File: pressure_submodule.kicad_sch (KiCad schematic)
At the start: 20 parts, among them IC11 PINA350ABSIDDFR, J13 Conn_01x04, Q11 BSZ0902NSATMA1

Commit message: WIP
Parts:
- renumbered C30 to C23, D12 to D5, F21 to F7, F22 to F8, IC11 to IC4, J13 to J6, JP71 to JP22, JP72 to JP23, JP73 to JP24, JP74 to JP25, JP75 to JP26, JP76 to JP27, JP77 to JP28, Q11 to Q4, R61 to R19, R62 to R20, R63 to R21, R64 to R22, R65 to R23, R66 to R24
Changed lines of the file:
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@@
   (symbol (lib_id "Device:R") (at 55.372 105.41 0)
     (in_bom yes) (on_board yes)
-    (property "Reference" "R63" (id 0) (at 51.562 105.283 0)
+    (property "Reference" "R21" (id 0) (at 51.562 105.283 0)
       (effects (font (size 1.27 1.27)) (justify left))
     )
@@
   (symbol (lib_id "TXV_Library_Symbols:BSZ0902NSATMA1") (at 162.052 74.549 0)
     (in_bom yes) (on_board yes)
-    (property "Reference" "Q11" (id 0) (at 165.989 74.549 0)
+    (property "Reference" "Q4" (id 0) (at 165.989 74.549 0)
       (effects (font (size 1.27 1.27)) (justify left))
     )
@@
   (symbol (lib_id "Jumper:Jumper_2_Open") (at 191.008 63.373 90)
     (in_bom yes) (on_board yes)
-    (property "Reference" "JP75" (id 0) (at 187.833 64.643 0)
+    (property "Reference" "JP26" (id 0) (at 187.833 64.643 0)
       (effects (font (size 1.27 1.27)) (justify left))
     )
@@
   (symbol (lib_id "Device:Polyfuse") (at 186.182 49.403 0)
     (in_bom yes) (on_board yes) (fields_autoplaced)
-    (property "Reference" "F21" (id 0) (at 188.595 48.1329 0)
+    (property "Reference" "F7" (id 0) (at 188.595 48.1329 0)
       (effects (font (size 1.27 1.27)) (justify left))
     )
@@
   (symbol (lib_id "TXV_Library_Symbols:PINA350ABSIDDFR") (at 99.822 92.075 180)
     (in_bom yes) (on_board yes) (fields_autoplaced)
-    (property "Reference" "IC11" (id 0) (at 85.852 76.962 0))
+    (property "Reference" "IC4" (id 0) (at 85.852 76.962 0))
     (property "Value" "PINA350ABSIDDFR" (id 1) (at 85.852 79.502 0))
     (property "Footprint" "TXV_Library_Footprints:SOT65P280X110-8N" (id 2) (at 75.692 94.615 0)
@@
   (symbol (lib_id "Jumper:Jumper_2_Open") (at 101.854 97.155 90)
     (in_bom yes) (on_board yes)
-    (property "Reference" "JP71" (id 0) (at 98.679 98.425 0)
+    (property "Reference" "JP22" (id 0) (at 98.679 98.425 0)
       (effects (font (size 1.27 1.27)) (justify left))
     )
@@
   (symbol (lib_id "Device:R") (at 163.322 91.567 0)
     (in_bom yes) (on_board yes)
-    (property "Reference" "R66" (id 0) (at 158.242 90.297 0)
+    (property "Reference" "R24" (id 0) (at 158.242 90.297 0)
       (effects (font (size 1.27 1.27)) (justify left))
     )
@@
   (symbol (lib_id "Device:C") (at 43.434 105.283 0)
     (in_bom yes) (on_board yes)
-    (property "Reference" "C30" (id 0) (at 39.37 103.505 0)
+    (property "Reference" "C23" (id 0) (at 39.37 103.505 0)
       (effects (font (size 1.27 1.27)) (justify left))
     )
@@
   (symbol (lib_id "Jumper:Jumper_2_Open") (at 191.008 73.533 90)
     (in_bom yes) (on_board yes)
-    (property "Reference" "JP76" (id 0) (at 187.833 74.803 0)
+    (property "Reference" "JP27" (id 0) (at 187.833 74.803 0)
       (effects (font (size 1.27 1.27)) (justify left))
     )
@@
   (symbol (lib_id "Jumper:Jumper_2_Open") (at 143.256 89.535 0)
     (in_bom yes) (on_board yes)
-    (property "Reference" "JP74" (id 0) (at 141.986 86.36 0)
+    (property "Reference" "JP25" (id 0) (at 141.986 86.36 0)
       (effects (font (size 1.27 1.27)) (justify left))
     )
@@
   (symbol (lib_id "Device:R") (at 143.637 74.549 90)
     (in_bom yes) (on_board yes)
-    (property "Reference" "R64" (id 0) (at 143.002 72.644 90)
+    (property "Reference" "R22" (id 0) (at 143.002 72.644 90)
       (effects (font (size 1.27 1.27)) (justify left))
     )
@@
   (symbol (lib_id "Jumper:Jumper_2_Open") (at 106.172 58.293 0)
     (in_bom yes) (on_board yes)
-    (property "Reference" "JP72" (id 0) (at 104.902 55.118 0)
+    (property "Reference" "JP23" (id 0) (at 104.902 55.118 0)
       (effects (font (size 1.27 1.27)) (justify left))
     )
@@
   (symbol (lib_id "Jumper:Jumper_2_Open") (at 113.03 64.643 90)
     (in_bom yes) (on_board yes)
-    (property "Reference" "JP73" (id 0) (at 109.855 65.913 0)
+    (property "Reference" "JP24" (id 0) (at 109.855 65.913 0)
       (effects (font (size 1.27 1.27)) (justify left))
     )
@@
   (symbol (lib_id "Device:D") (at 170.942 73.914 270)
     (in_bom yes) (on_board yes)
-    (property "Reference" "D12" (id 0) (at 172.9486 72.7456 90)
+    (property "Reference" "D5" (id 0) (at 172.9486 72.7456 90)
       (effects (font (size 1.27 1.27)) (justify left))
     )
@@
   (symbol (lib_id "Device:Polyfuse") (at 200.152 49.403 0)
     (in_bom yes) (on_board yes) (fields_autoplaced)
-    (property "Reference" "F22" (id 0) (at 202.565 48.1329 0)
+    (property "Reference" "F8" (id 0) (at 202.565 48.1329 0)
       (effects (font (size 1.27 1.27)) (justify left))
     )
@@
   (symbol (lib_id "Connector_Generic:Conn_01x04") (at 213.106 58.293 0)
     (in_bom yes) (on_board yes)
-    (property "Reference" "J13" (id 0) (at 215.138 58.4962 0)
+    (property "Reference" "J6" (id 0) (at 215.138 58.4962 0)
       (effects (font (size 1.27 1.27)) (justify left))
     )
@@
   (symbol (lib_id "Device:R") (at 151.892 79.629 0)
     (in_bom yes) (on_board yes)
-    (property "Reference" "R65" (id 0) (at 145.542 78.359 0)
+    (property "Reference" "R23" (id 0) (at 145.542 78.359 0)
       (effects (font (size 1.27 1.27)) (justify left))
     )
@@
   (symbol (lib_id "Device:R") (at 55.372 95.25 0)
     (in_bom yes) (on_board yes)
-    (property "Reference" "R62" (id 0) (at 50.292 93.345 0)
+    (property "Reference" "R20" (id 0) (at 50.292 93.345 0)
       (effects (font (size 1.27 1.27)) (justify left))
     )
@@
   (symbol (lib_id "Jumper:Jumper_2_Open") (at 204.216 69.977 90)
     (in_bom yes) (on_board yes)
-    (property "Reference" "JP77" (id 0) (at 201.041 71.247 0)
+    (property "Reference" "JP28" (id 0) (at 201.041 71.247 0)
       (effects (font (size 1.27 1.27)) (justify left))
     )
@@
   (symbol (lib_id "Device:R") (at 49.53 100.457 90)
     (in_bom yes) (on_board yes)
-    (property "Reference" "R61" (id 0) (at 50.292 102.489 90)
-      (effects (font (size 1.27 1.27)) (justify left))
-    )
+    (property "Reference" "R19" (id 0) (at 50.292 102.489 90)
+      (effects (font (size 1.27 1.27)) (justify left))
+    )

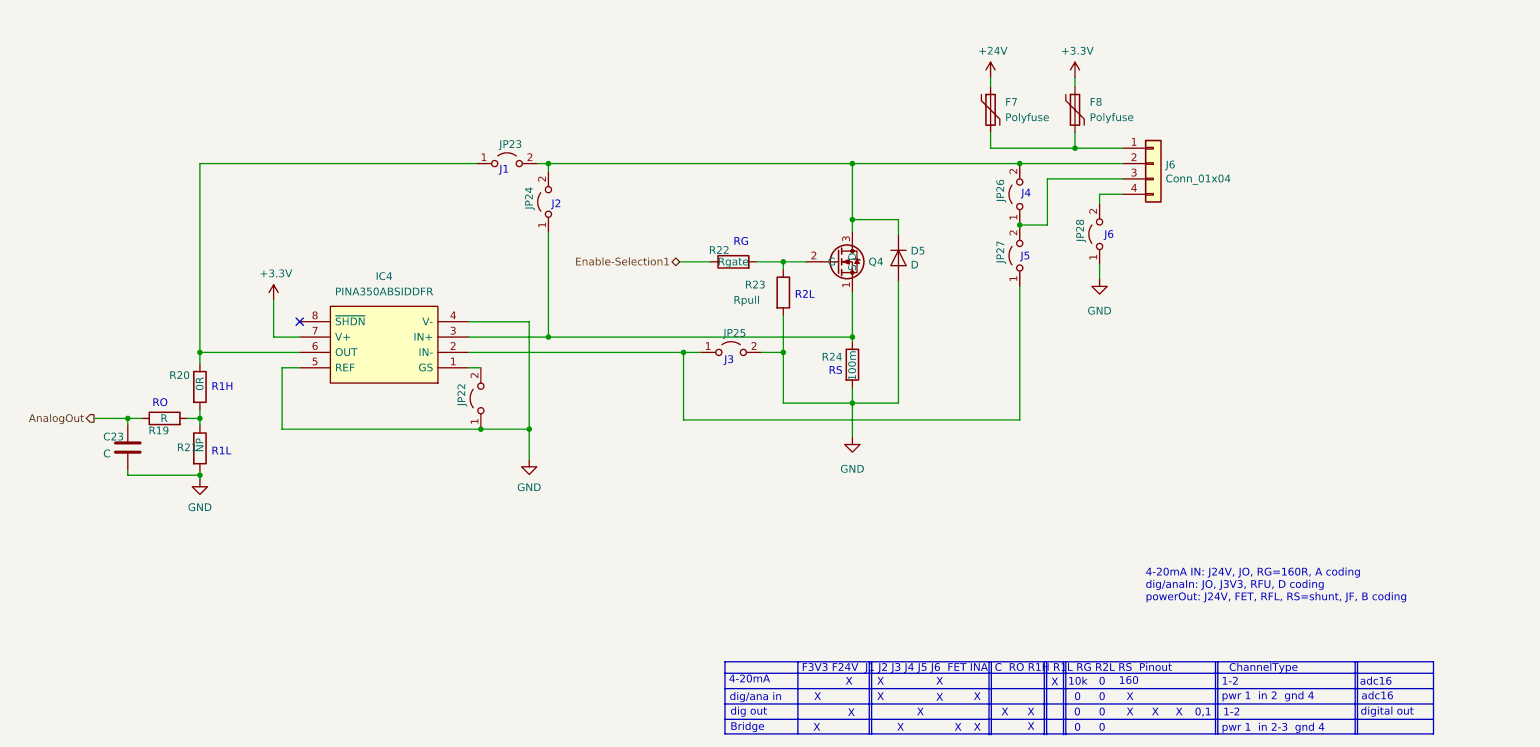
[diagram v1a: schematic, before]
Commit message: UART5 add
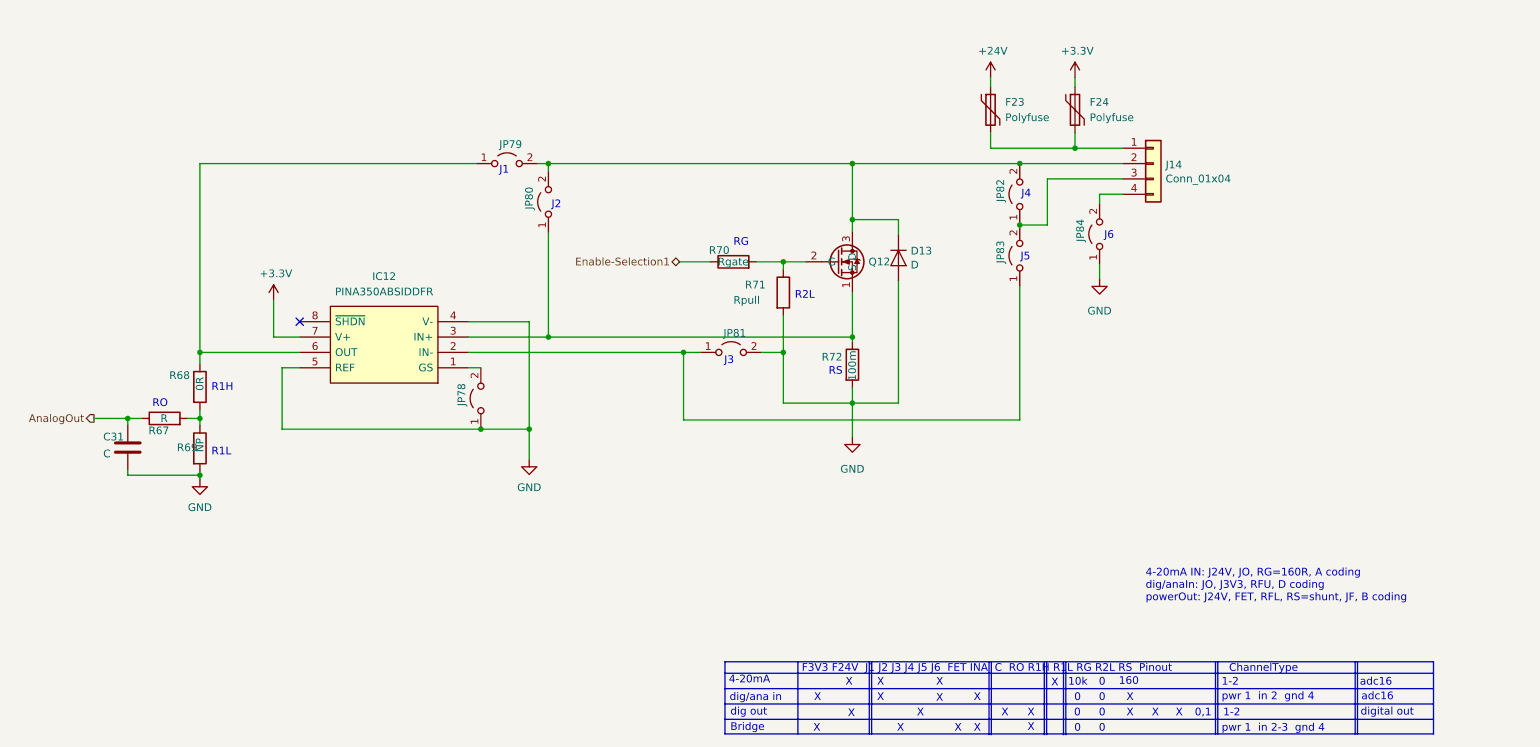
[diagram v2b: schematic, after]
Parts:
- renumbered C23 to C31, D5 to D13, F7 to F23, F8 to F24, IC4 to IC12, J6 to J14, JP22 to JP78, JP23 to JP79, JP24 to JP80, JP25 to JP81, JP26 to JP82, JP27 to JP83, JP28 to JP84, Q4 to Q12, R19 to R67, R20 to R68, R21 to R69, R22 to R70, R23 to R71, R24 to R72
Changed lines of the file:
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@@
   (symbol (lib_id "Device:R") (at 55.372 105.41 0)
     (in_bom yes) (on_board yes)
-    (property "Reference" "R21" (id 0) (at 51.562 105.283 0)
+    (property "Reference" "R69" (id 0) (at 51.562 105.283 0)
       (effects (font (size 1.27 1.27)) (justify left))
     )
@@
   (symbol (lib_id "TXV_Library_Symbols:BSZ0902NSATMA1") (at 162.052 74.549 0)
     (in_bom yes) (on_board yes)
-    (property "Reference" "Q4" (id 0) (at 165.989 74.549 0)
+    (property "Reference" "Q12" (id 0) (at 165.989 74.549 0)
       (effects (font (size 1.27 1.27)) (justify left))
     )
@@
   (symbol (lib_id "Jumper:Jumper_2_Open") (at 191.008 63.373 90)
     (in_bom yes) (on_board yes)
-    (property "Reference" "JP26" (id 0) (at 187.833 64.643 0)
+    (property "Reference" "JP82" (id 0) (at 187.833 64.643 0)
       (effects (font (size 1.27 1.27)) (justify left))
     )
@@
   (symbol (lib_id "Device:Polyfuse") (at 186.182 49.403 0)
     (in_bom yes) (on_board yes) (fields_autoplaced)
-    (property "Reference" "F7" (id 0) (at 188.595 48.1329 0)
+    (property "Reference" "F23" (id 0) (at 188.595 48.1329 0)
       (effects (font (size 1.27 1.27)) (justify left))
     )
@@
   (symbol (lib_id "TXV_Library_Symbols:PINA350ABSIDDFR") (at 99.822 92.075 180)
     (in_bom yes) (on_board yes) (fields_autoplaced)
-    (property "Reference" "IC4" (id 0) (at 85.852 76.962 0))
+    (property "Reference" "IC12" (id 0) (at 85.852 76.962 0))
     (property "Value" "PINA350ABSIDDFR" (id 1) (at 85.852 79.502 0))
     (property "Footprint" "TXV_Library_Footprints:SOT65P280X110-8N" (id 2) (at 75.692 94.615 0)
@@
   (symbol (lib_id "Jumper:Jumper_2_Open") (at 101.854 97.155 90)
     (in_bom yes) (on_board yes)
-    (property "Reference" "JP22" (id 0) (at 98.679 98.425 0)
+    (property "Reference" "JP78" (id 0) (at 98.679 98.425 0)
       (effects (font (size 1.27 1.27)) (justify left))
     )
@@
   (symbol (lib_id "Device:R") (at 163.322 91.567 0)
     (in_bom yes) (on_board yes)
-    (property "Reference" "R24" (id 0) (at 158.242 90.297 0)
+    (property "Reference" "R72" (id 0) (at 158.242 90.297 0)
       (effects (font (size 1.27 1.27)) (justify left))
     )
@@
   (symbol (lib_id "Device:C") (at 43.434 105.283 0)
     (in_bom yes) (on_board yes)
-    (property "Reference" "C23" (id 0) (at 39.37 103.505 0)
+    (property "Reference" "C31" (id 0) (at 39.37 103.505 0)
       (effects (font (size 1.27 1.27)) (justify left))
     )
@@
   (symbol (lib_id "Jumper:Jumper_2_Open") (at 191.008 73.533 90)
     (in_bom yes) (on_board yes)
-    (property "Reference" "JP27" (id 0) (at 187.833 74.803 0)
+    (property "Reference" "JP83" (id 0) (at 187.833 74.803 0)
       (effects (font (size 1.27 1.27)) (justify left))
     )
@@
   (symbol (lib_id "Jumper:Jumper_2_Open") (at 143.256 89.535 0)
     (in_bom yes) (on_board yes)
-    (property "Reference" "JP25" (id 0) (at 141.986 86.36 0)
+    (property "Reference" "JP81" (id 0) (at 141.986 86.36 0)
       (effects (font (size 1.27 1.27)) (justify left))
     )
@@
   (symbol (lib_id "Device:R") (at 143.637 74.549 90)
     (in_bom yes) (on_board yes)
-    (property "Reference" "R22" (id 0) (at 143.002 72.644 90)
+    (property "Reference" "R70" (id 0) (at 143.002 72.644 90)
       (effects (font (size 1.27 1.27)) (justify left))
     )
@@
   (symbol (lib_id "Jumper:Jumper_2_Open") (at 106.172 58.293 0)
     (in_bom yes) (on_board yes)
-    (property "Reference" "JP23" (id 0) (at 104.902 55.118 0)
+    (property "Reference" "JP79" (id 0) (at 104.902 55.118 0)
       (effects (font (size 1.27 1.27)) (justify left))
     )
@@
   (symbol (lib_id "Jumper:Jumper_2_Open") (at 113.03 64.643 90)
     (in_bom yes) (on_board yes)
-    (property "Reference" "JP24" (id 0) (at 109.855 65.913 0)
+    (property "Reference" "JP80" (id 0) (at 109.855 65.913 0)
       (effects (font (size 1.27 1.27)) (justify left))
     )
@@
   (symbol (lib_id "Device:D") (at 170.942 73.914 270)
     (in_bom yes) (on_board yes)
-    (property "Reference" "D5" (id 0) (at 172.9486 72.7456 90)
+    (property "Reference" "D13" (id 0) (at 172.9486 72.7456 90)
       (effects (font (size 1.27 1.27)) (justify left))
     )
@@
   (symbol (lib_id "Device:Polyfuse") (at 200.152 49.403 0)
     (in_bom yes) (on_board yes) (fields_autoplaced)
-    (property "Reference" "F8" (id 0) (at 202.565 48.1329 0)
+    (property "Reference" "F24" (id 0) (at 202.565 48.1329 0)
       (effects (font (size 1.27 1.27)) (justify left))
     )
@@
   (symbol (lib_id "Connector_Generic:Conn_01x04") (at 213.106 58.293 0)
     (in_bom yes) (on_board yes)
-    (property "Reference" "J6" (id 0) (at 215.138 58.4962 0)
+    (property "Reference" "J14" (id 0) (at 215.138 58.4962 0)
       (effects (font (size 1.27 1.27)) (justify left))
     )
@@
   (symbol (lib_id "Device:R") (at 151.892 79.629 0)
     (in_bom yes) (on_board yes)
-    (property "Reference" "R23" (id 0) (at 145.542 78.359 0)
+    (property "Reference" "R71" (id 0) (at 145.542 78.359 0)
       (effects (font (size 1.27 1.27)) (justify left))
     )
@@
   (symbol (lib_id "Device:R") (at 55.372 95.25 0)
     (in_bom yes) (on_board yes)
-    (property "Reference" "R20" (id 0) (at 50.292 93.345 0)
+    (property "Reference" "R68" (id 0) (at 50.292 93.345 0)
       (effects (font (size 1.27 1.27)) (justify left))
     )
@@
   (symbol (lib_id "Jumper:Jumper_2_Open") (at 204.216 69.977 90)
     (in_bom yes) (on_board yes)
-    (property "Reference" "JP28" (id 0) (at 201.041 71.247 0)
+    (property "Reference" "JP84" (id 0) (at 201.041 71.247 0)
       (effects (font (size 1.27 1.27)) (justify left))
     )
@@
   (symbol (lib_id "Device:R") (at 49.53 100.457 90)
     (in_bom yes) (on_board yes)
-    (property "Reference" "R19" (id 0) (at 50.292 102.489 90)
-      (effects (font (size 1.27 1.27)) (justify left))
-    )
+    (property "Reference" "R67" (id 0) (at 50.292 102.489 90)
+      (effects (font (size 1.27 1.27)) (justify left))
+    )

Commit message: WIP
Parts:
- renumbered C31 to C20, D13 to D2, F23 to F1, F24 to F2, IC12 to IC1, J14 to J3, JP78 to JP1, JP79 to JP2, JP80 to JP3, JP81 to JP4, JP82 to JP5, JP83 to JP6, JP84 to JP7, Q12 to Q1, R67 to R1, R68 to R2, R69 to R3, R70 to R4, R71 to R5, R72 to R6
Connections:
- net +3V3 renamed +3.3V

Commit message: Almost ready to be ordered
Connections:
- net +3.3V renamed +3V3
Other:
- moved on the sheet: C20, D2, F1, F2, IC1, J3, JP1, JP2, JP3, JP4, JP5, JP6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

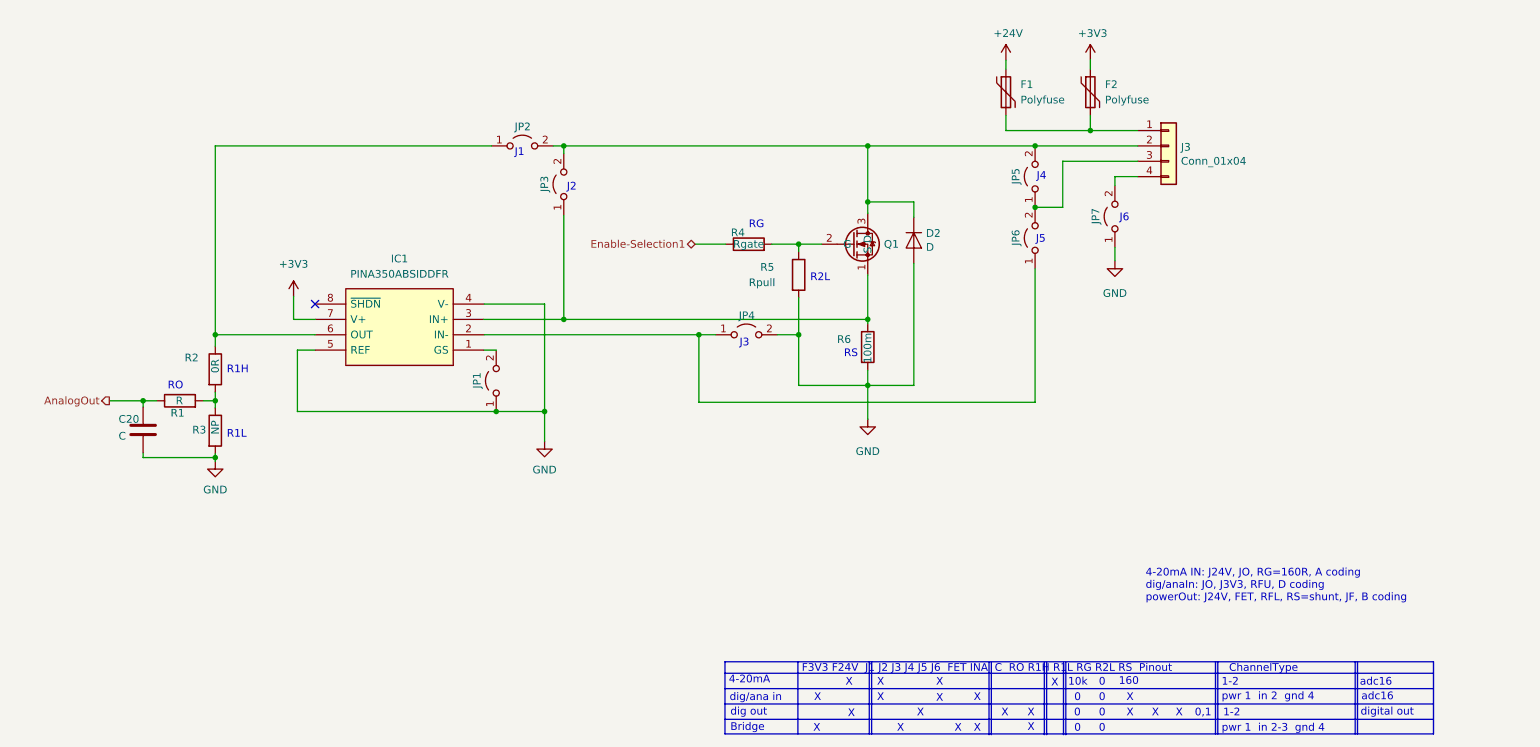
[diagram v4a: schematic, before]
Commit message: Added Servo Config
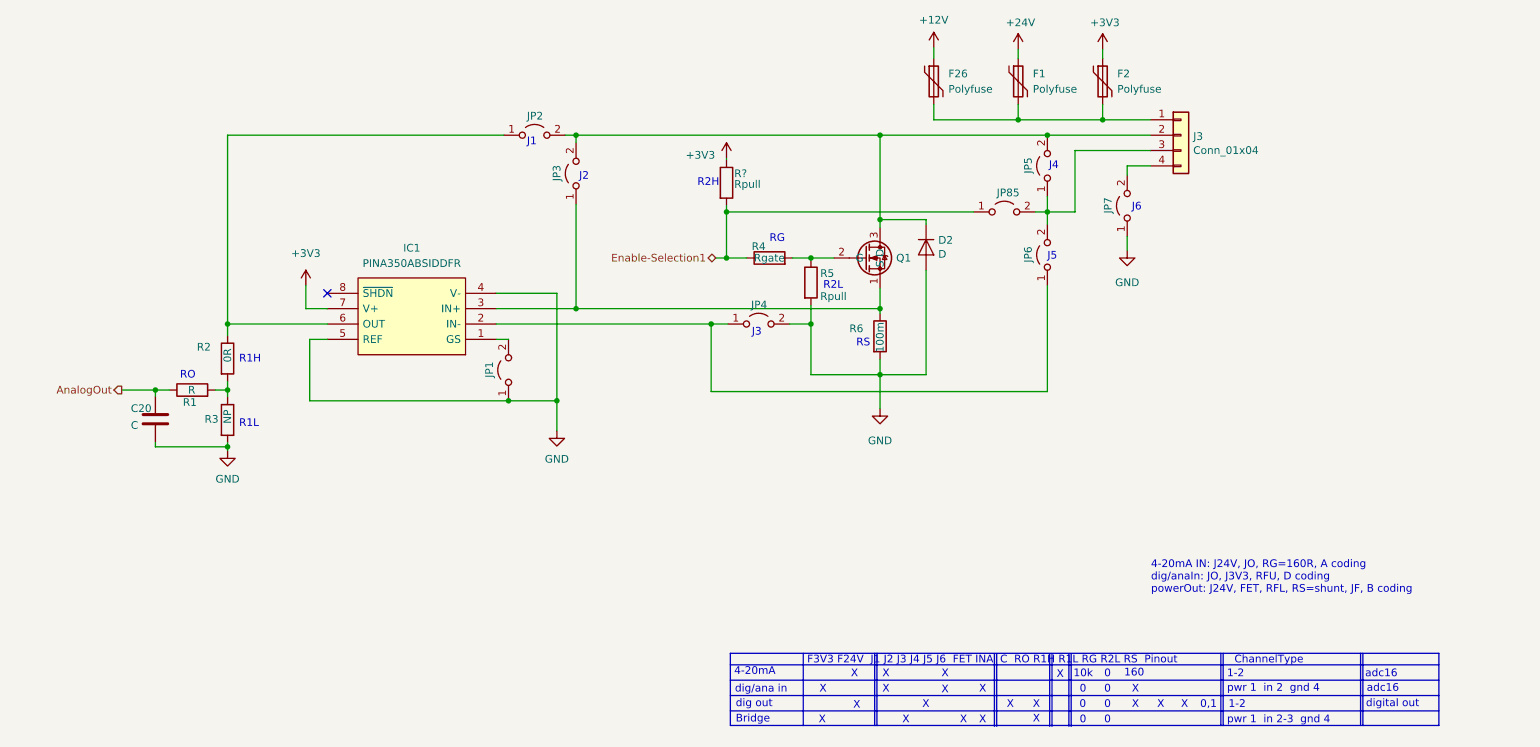
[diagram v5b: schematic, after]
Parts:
- added F26: Polyfuse, Fuse:Fuse_0805_2012Metric, symbol Device:Polyfuse
- added JP85: Jumper_2_Open, Jumper:SolderJumper-2_P1.3mm_Open_TrianglePad1.0x1.5mm, symbol Jumper:Jumper_2_Open
- added R?: Rpull, Resistor_SMD:R_0603_1608Metric, symbol Device:R
- F1, F2: footprint TXV_Library_Footprints:0805L110SL PPTC Polyfuse Littelfuse -> Fuse:Fuse_0805_2012Metric
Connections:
- net +3V3: now also R?.1
- net Enable-Selection1: now also JP85.1 (A), R?.2
- net at J3.3 (Pin_3), JP5.1 (A), JP6.2 (B): now also JP85.2 (B)
- net at F1.2, F2.2, J3.1 (Pin_1): now also F26.2
- new net +12V: F26.1
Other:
- note added: "R2H"
- moved on the sheet: C20, D2, F1, F2, IC1, J3, JP1, JP2, JP3, JP4, JP5, JP6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
